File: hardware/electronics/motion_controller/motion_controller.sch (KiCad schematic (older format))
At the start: 149 parts

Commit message: Fixed motion controller schem. so that design rules check is satisfied. Addd 2nd resistor to differential amplifier - to make it easy to find components with correct  values.
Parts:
- removed U? (x10): MAX4505, symbol MAX4505
- added K5: CONN_3, symbol CONN_3
- added P1: CONN_2, symbol CONN_2
- added R56, R57, R58, R59, R60, R61, R62, R63, R64, R65: 191, ~, symbol R
- added U11, U13, U15, U17, U19, U21, U23, U25, U7, U9: MAX4505, ~, symbol MAX4505
- C1, C10, C11, C12, C13, C14, C15, C16, C17, C18, C19, C2, C20, C21, C22, C23, C24, C25, C3, C4, C5, C6, C7, C8, C9: renamed from C?; value C -> 0.1uF
- R10, R17, R22, R28, R33, R38, R43, R49, R5, R55: renamed from R?; value 3.191k -> 3k
- R14, R15, R53: renamed from R?; value R -> 4.7k
- R27: renamed from R?; value R -> 3.3k
- R47: renamed from R?; value R -> 500
- gave numbers to parts that had none: 99
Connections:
- net 3V3_TNY: now also U11.2 (V+), U13.2 (V+), U15.2 (V+), U17.2 (V+), U19.2 (V+), U21.2 (V+), U23.2 (V+), U25.2 (V+), U7.2 (V+), U9.2 (V+)
- net 5V_SEL: now also K5.2 (PM)
- net AOUT: now also P1.1 (P1)
- net DIR0_INV: no longer P20.3
- net DIR0_SEL: no longer P20.2, P20.4
- net DIR1_INV: now also P20.3
- net DIR1_SEL: now also P20.2, P20.4
- net GND: now also P29.2 (PM), K5.3 (P3), P1.2 (PM), R56.1, R57.1, R58.1, R59.1, R60.1, R61.1, R62.1, R63.1, R64.1, R65.1, U11.5 (V-), U13.5 (V-), U15.5 (V-), U17.5 (V-), U19.5 (V-), U21.5 (V-), U23.5 (V-), U25.5 (V-), U7.5 (V-), U9.5 (V-); no longer R10.1, R17.1, R22.1, R28.1, R33.1, R38.1, R43.1, R49.1, R5.1, R55.1
- net INT0: now also P13.1 (P1), P14.1 (P1), P15.1 (P1), P16.1 (P1), P17.1 (P1), P18.1 (P1), R27.1
- net SG0: now also U7.3 (AOUT)
- net SG1: now also U9.3 (AOUT)
- net SG2: now also U11.3 (AOUT)
- net SG3: now also U13.3 (AOUT)
- net SG4: now also U15.3 (AOUT)
- net SG5: now also U17.3 (AOUT)
- net SG6: now also U19.3 (AOUT)
- net SG7: now also U21.3 (AOUT)
- net SG8: now also U23.3 (AOUT)
- net SG9: now also U25.3 (AOUT)
- net at R1.2, U8.6 (OUT): now also U7.1 (AIN)
- net at R6.2, U10.6 (OUT): now also U9.1 (AIN)
- net at R11.2, U12.6 (OUT): now also U11.1 (AIN)
- net at R18.2, U14.6 (OUT): now also U13.1 (AIN)
- net at R23.2, U16.6 (OUT): now also U15.1 (AIN)
- net at R29.2, U18.6 (OUT): now also U17.1 (AIN)
- net at R34.2, U20.6 (OUT): now also U19.1 (AIN)
- net at R39.2, U22.6 (OUT): now also U21.1 (AIN)
- net at R44.2, U24.6 (OUT): now also U23.1 (AIN)
- net at R50.2, U26.6 (OUT): now also U25.1 (AIN)
- net D10,CS renamed PWM4,D10,CS
- net PWM4,D10,CS: now also K5.1 (P1)
- new net: R5.1, R56.2
- new net: R10.1, R57.2
- new net: R17.1, R58.2
- new net: R22.1, R59.2
- new net: R28.1, R60.2
- new net: R33.1, R61.2
- new net: R38.1, R62.2
- new net: R43.1, R63.2
- new net: R49.1, R64.2
- new net: R55.1, R65.2
- no-connect marks 97 -> 98
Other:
- note added: "Analog Output (0-3.3V)"
- note added: "Direction Select (Mirrored Axes)"
- note added: "PWM, RC Servos"
- note removed: "RC Servos"
- moved on the sheet: C1, C10, C11, C12, C13, C14, C15, C16, C17, C18, C19, C2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

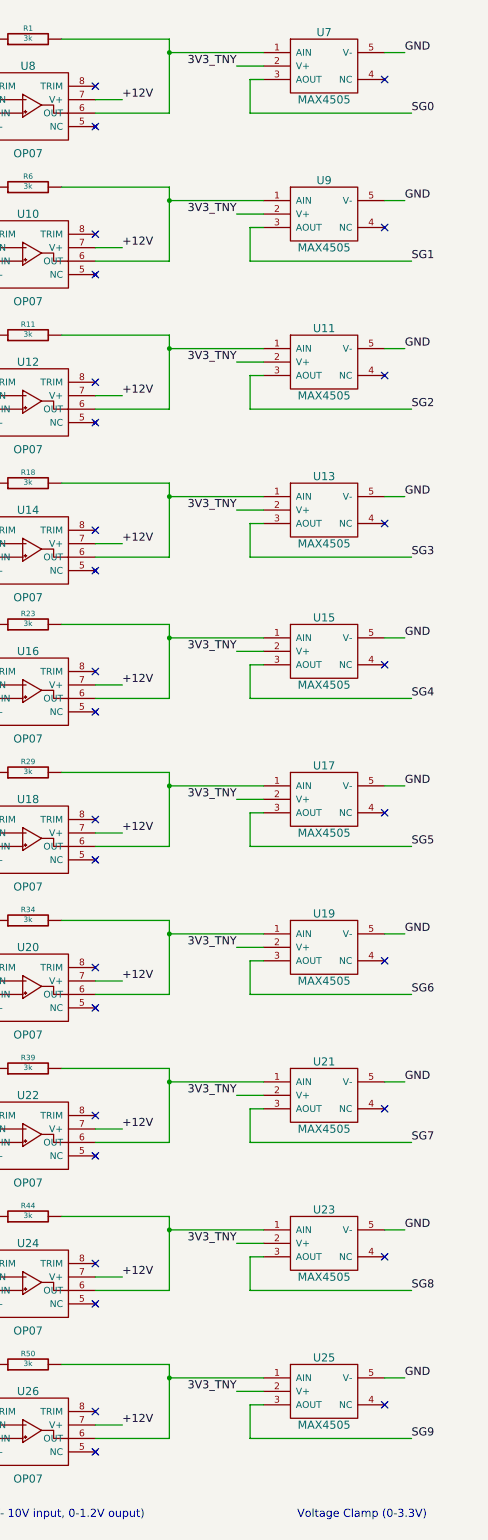
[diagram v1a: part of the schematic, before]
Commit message: Changed clamping circuit. Worked on footprint assignment.
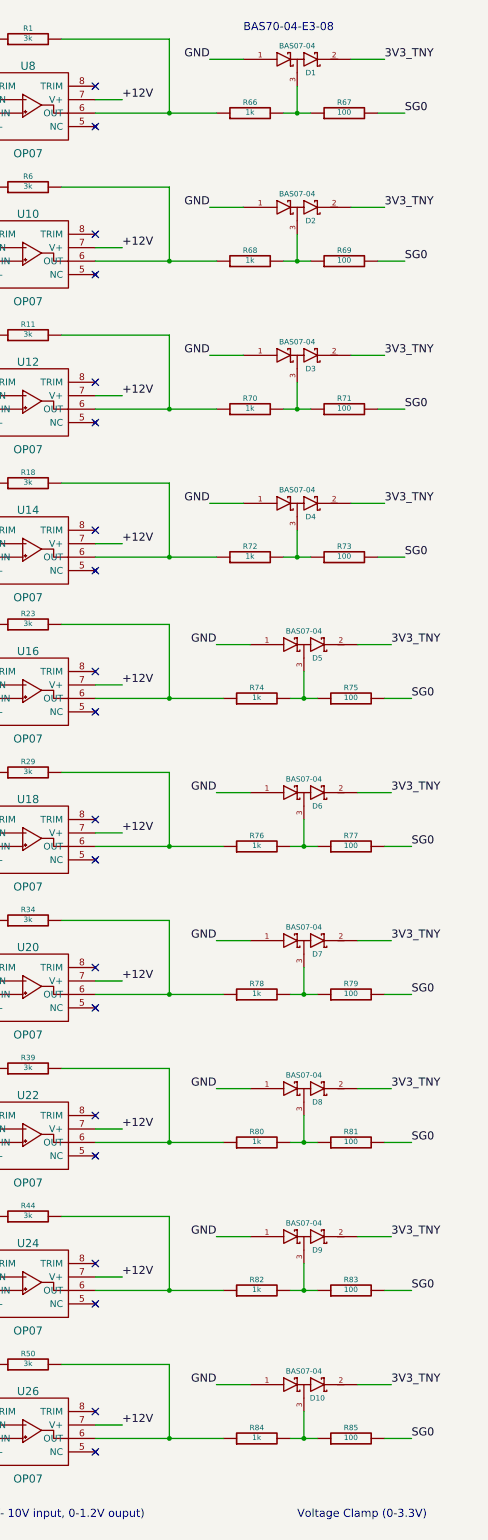
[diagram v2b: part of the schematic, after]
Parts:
- removed U11, U13, U15, U17, U19, U21, U23, U25, U7, U9: MAX4505, ~, symbol MAX4505
- added D1, D10, D2, D3, D4, D5, D6, D7, D8, D9: BAS07-04, ~, symbol BAS07-04
- added R66, R68, R70, R72, R74, R76, R78, R80, R82, R84: 1k, ~, symbol R
- added R67, R69, R71, R73, R75, R77, R79, R81, R83, R85: 100, ~, symbol R
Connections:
- net 3V3_TNY: now also D1.2 (cathode), D10.2 (cathode), D2.2 (cathode), D3.2 (cathode), D4.2 (cathode), D5.2 (cathode), D6.2 (cathode), D7.2 (cathode), D8.2 (cathode), D9.2 (cathode)
- net GND: now also D1.1 (Anode), D10.1 (Anode), D2.1 (Anode), D3.1 (Anode), D4.1 (Anode), D5.1 (Anode), D6.1 (Anode), D7.1 (Anode), D8.1 (Anode), D9.1 (Anode)
- net SG0: now also R67.2, R69.2, R71.2, R73.2, R75.2, R77.2, R79.2, R81.2, R83.2, R85.2
- net at R1.2, U8.6 (OUT): now also R66.1
- net at R6.2, U10.6 (OUT): now also R68.1
- net at R11.2, U12.6 (OUT): now also R70.1
- net at R18.2, U14.6 (OUT): now also R72.1
- net at R23.2, U16.6 (OUT): now also R74.1
- net at R29.2, U18.6 (OUT): now also R76.1
- net at R34.2, U20.6 (OUT): now also R78.1
- net at R39.2, U22.6 (OUT): now also R80.1
- net at R44.2, U24.6 (OUT): now also R82.1
- net at R50.2, U26.6 (OUT): now also R84.1
- new net: D1.3 (AK), R66.2, R67.1
- new net: D2.3 (AK), R68.2, R69.1
- new net: D3.3 (AK), R70.2, R71.1
- new net: D4.3 (AK), R72.2, R73.1
- new net: D5.3 (AK), R74.2, R75.1
- new net: D6.3 (AK), R76.2, R77.1
- new net: D7.3 (AK), R78.2, R79.1
- new net: D8.3 (AK), R80.2, R81.1
- new net: D9.3 (AK), R82.2, R83.1
- new net: D10.3 (AK), R84.2, R85.1
- no-connect marks 98 -> 88
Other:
- note added: "BAS70-04-E3-08"
